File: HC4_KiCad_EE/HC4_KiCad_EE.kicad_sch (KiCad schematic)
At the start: 13 parts, among them IC2 ROM, J1 Power

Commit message: 仕様決め
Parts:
- added U1: ATmega4809-A, Package_QFP:TQFP-48_7x7mm_P0.5mm, symbol MCU_Microchip_ATmega:ATmega4809-A
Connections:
- new net: U1.14 (VCC), U1.42 (VCC)
- new net: U1.15 (GND), U1.29 (GND), U1.43 (GND)
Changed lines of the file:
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@@
+	)
+	(symbol
+		(lib_id "MCU_Microchip_ATmega:ATmega4809-A")
+		(at 52.07 96.52 0)
+		(unit 1)
+		(exclude_from_sim no)
+		(in_bom yes)
+		(on_board yes)
+		(dnp no)
+		(fields_autoplaced yes)
+		(property "Reference" "U1"
+			(at 54.2133 132.08 0)
+			(effects
+				(font
+					(size 1.27 1.27)
+				)
+				(justify left)
+			)
+		)
+		(property "Value" "ATmega4809-A"
+			(at 54.2133 134.62 0)
+			(effects
+				(font
+					(size 1.27 1.27)
+				)
+				(justify left)
+			)
+		)
+		(property "Footprint" "Package_QFP:TQFP-48_7x7mm_P0.5mm"
+			(at 52.07 96.52 0)
+			(effects
+				(font
+					(size 1.27 1.27)
+					(italic yes)
+				)
+				(hide yes)
+			)
+		)
+		(property "Datasheet" "http://ww1.microchip.com/downloads/en/DeviceDoc/40002016A.pdf"
+			(at 52.07 96.52 0)
+			(effects
+				(font
+					(size 1.27 1.27)
+				)
+				(hide yes)
+			)
+		)
+		(property "Description" "20MHz, 48kB Flash, 6kB SRAM, 256B EEPROM, TQFP-48"
+			(at 52.07 96.52 0)
+			(effects
+				(font
+					(size 1.27 1.27)
+				)
+				(hide yes)
+			)
+		)
+		(pin "32"
+		)
+		(pin "25"
+		)
+		(pin "21"
+		)
+		(pin "42"
+		)
+		(pin "29"
+		)
+		(pin "28"
+		)
+		(pin "34"
+		)
+		(pin "45"
+		)
+		(pin "37"
+		)
+		(pin "46"
+		)
+		(pin "31"
+		)
+		(pin "26"
+		)
+		(pin "40"
+		)
+		(pin "33"
+		)
+		(pin "35"
+		)
+		(pin "39"
+		)
+		(pin "41"
+		)
+		(pin "36"
+		)
+		(pin "30"
+		)
+		(pin "23"
+		)
+		(pin "38"
+		)
+		(pin "20"
+		)
+		(pin "22"
+		)
+		(pin "24"
+		)
+		(pin "27"
+		)
+		(pin "14"
+		)
+		(pin "15"
+		)
+		(pin "43"
+		)
+		(pin "44"
+		)
+		(pin "9"
+		)
+		(pin "11"
+		)
+		(pin "12"
+		)
+		(pin "47"
+		)
+		(pin "48"
+		)
+		(pin "8"
+		)
+		(pin "4"
+		)
+		(pin "13"
+		)
+		(pin "16"
+		)
+		(pin "10"
+		)
+		(pin "2"
+		)
+		(pin "3"
+		)
+		(pin "5"
+		)
+		(pin "6"
+		)
+		(pin "1"
+		)
+		(pin "7"
+		)
+		(pin "17"
+		)
+		(pin "18"
+		)
+		(pin "19"
+		)
+		(instances
+			(project ""
+				(path "/33731ded-38c0-4297-bdd8-92b082f46ff8"
+					(reference "U1")
+					(unit 1)
+				)
+			)
+		)
 	)
 	(symbol

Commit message: 一部を整地
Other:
- sheet Data BUS ports: added none; removed BUS_Zero, Databus[0..3], Level_C_OE, RAM_A[0..7], ~{RD}, ~{WR}
- sheet Instruction Decoder ports: added none; removed BUS_Zero, LevelC_OE
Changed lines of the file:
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@@
 	(bus
 		(pts
-			(xy 76.2 39.37) (xy 76.2 57.15)
-		)
-		(stroke
-			(width 0)
-			(type default)
-		)
-	)
-	(bus
-		(pts
 			(xy 254 71.12) (xy 254 93.98)
 		)
@@
 	(wire
 		(pts
-			(xy 60.96 49.53) (xy 60.96 39.37)
-		)
-		(stroke
-			(width 0)
-			(type default)
-		)
-	)
-	(bus
-		(pts
-			(xy 55.88 44.45) (xy 27.94 44.45)
-		)
-		(stroke
-			(width 0)
-			(type default)
-		)
-	)
-	(wire
-		(pts
 			(xy 43.18 171.45) (xy 48.26 171.45)
 		)
@@
 		)
 	)
-	(wire
-		(pts
-			(xy 203.2 39.37) (xy 203.2 48.26)
-		)
-		(stroke
-			(width 0)
-			(type default)
-		)
-	)
 	(polyline
 		(pts
@@
 		)
 	)
-	(bus
-		(pts
-			(xy 27.94 44.45) (xy 27.94 57.15)
-		)
-		(stroke
-			(width 0)
-			(type default)
-		)
-	)
 	(wire
 		(pts
@@
 		)
 	)
-	(wire
-		(pts
-			(xy 189.23 39.37) (xy 189.23 48.26)
-		)
-		(stroke
-			(width 0)
-			(type default)
-		)
-	)
 	(bus
 		(pts
@@
 	(bus
 		(pts
-			(xy 55.88 39.37) (xy 55.88 44.45)
-		)
-		(stroke
-			(width 0)
-			(type default)
-		)
-	)
-	(bus
-		(pts
 			(xy 116.84 81.28) (xy 116.84 83.82)
 		)
@@
 		)
 	)
-	(wire
-		(pts
-			(xy 58.42 39.37) (xy 58.42 52.07)
-		)
-		(stroke
-			(width 0)
-			(type default)
-		)
-	)
 	(bus
 		(pts
@@
 			)
 		)
-		(pin "BUS_Zero" input
-			(at 203.2 48.26 90)
-			(effects
-				(font
-					(size 1.27 1.27)
-				)
-				(justify right)
-			)
-		)
 		(pin "Zero_Flg" output
 			(at 238.76 59.69 0)
@@
 			)
 		)
-		(pin "LevelC_OE" output
-			(at 189.23 48.26 90)
-			(effects
-				(font
-					(size 1.27 1.27)
-				)
-				(justify right)
-			)
-		)
 		(pin "~{RAM_WR}" output
 			(at 201.93 76.2 270)
@@
 			)
 		)
-		(pin "ALU[0..3]" input
-			(at 91.44 39.37 270)
-			(effects
-				(font
-					(size 1.27 1.27)
-				)
-				(justify left)
-			)
-		)
-		(pin "Databus[0..3]" bidirectional
-			(at 76.2 39.37 270)
-			(effects
-				(font
-					(size 1.27 1.27)
-				)
-				(justify left)
-			)
-		)
 		(pin "Stack[0..3]" output
 			(at 105.41 39.37 270)
@@
 			)
 		)
-		(pin "~{ALU_OE}" input
-			(at 186.69 39.37 270)
-			(effects
-				(font
-					(size 1.27 1.27)
-				)
-				(justify left)
-			)
-		)
 		(pin "~{Immediate_OE}" input
 			(at 191.77 39.37 270)
@@
 			)
 		)
-		(pin "BUS_Zero" output
-			(at 203.2 39.37 270)
-			(effects
-				(font
-					(size 1.27 1.27)
-				)
-				(justify left)
-			)
-		)
-		(pin "RAM_A[0..7]" input
-			(at 55.88 39.37 270)
-			(effects
-				(font
-					(size 1.27 1.27)
-				)
-				(justify left)
-			)
-		)
-		(pin "~{RD}" input
-			(at 58.42 39.37 270)
-			(effects
-				(font
-					(size 1.27 1.27)
-				)
-				(justify left)
-			)
-		)
-		(pin "~{WR}" input
-			(at 60.96 39.37 270)
+		(pin "ALU[0..3]" input
+			(at 91.44 39.37 270)
 			(effects
 				(font
@@
 			)
 		)
-		(pin "Level_C_OE" input
-			(at 189.23 39.37 270)
+		(pin "~{ALU_OE}" input
+			(at 186.69 39.37 270)
 			(effects
 				(font

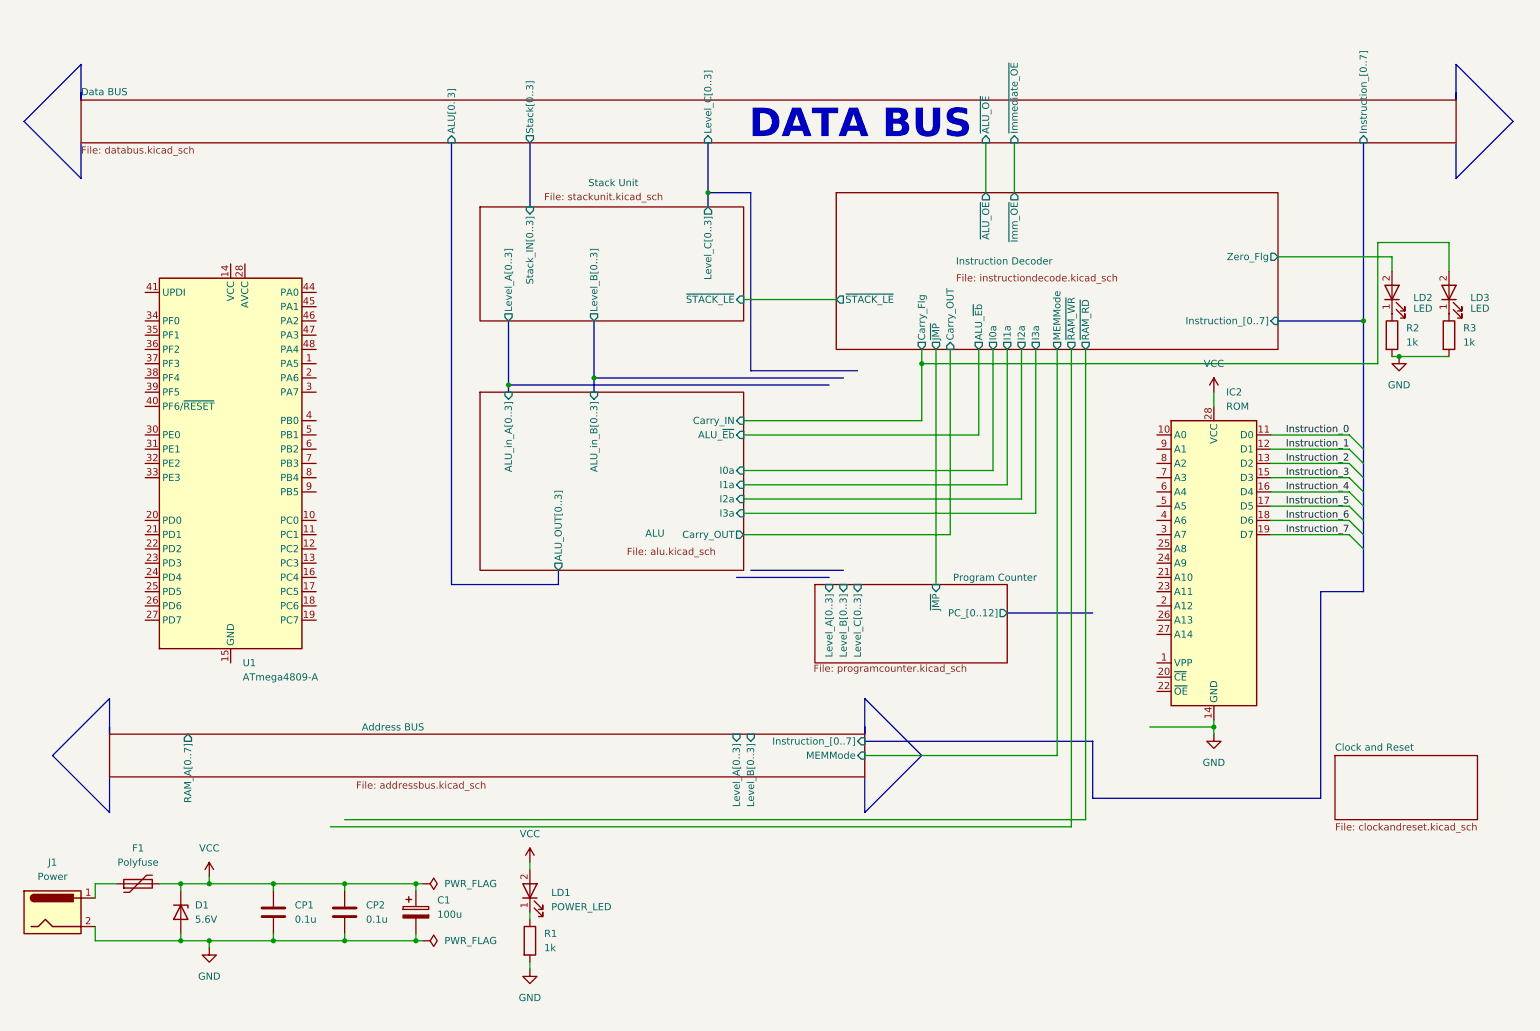
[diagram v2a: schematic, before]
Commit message: 4809を別シートに、ほか
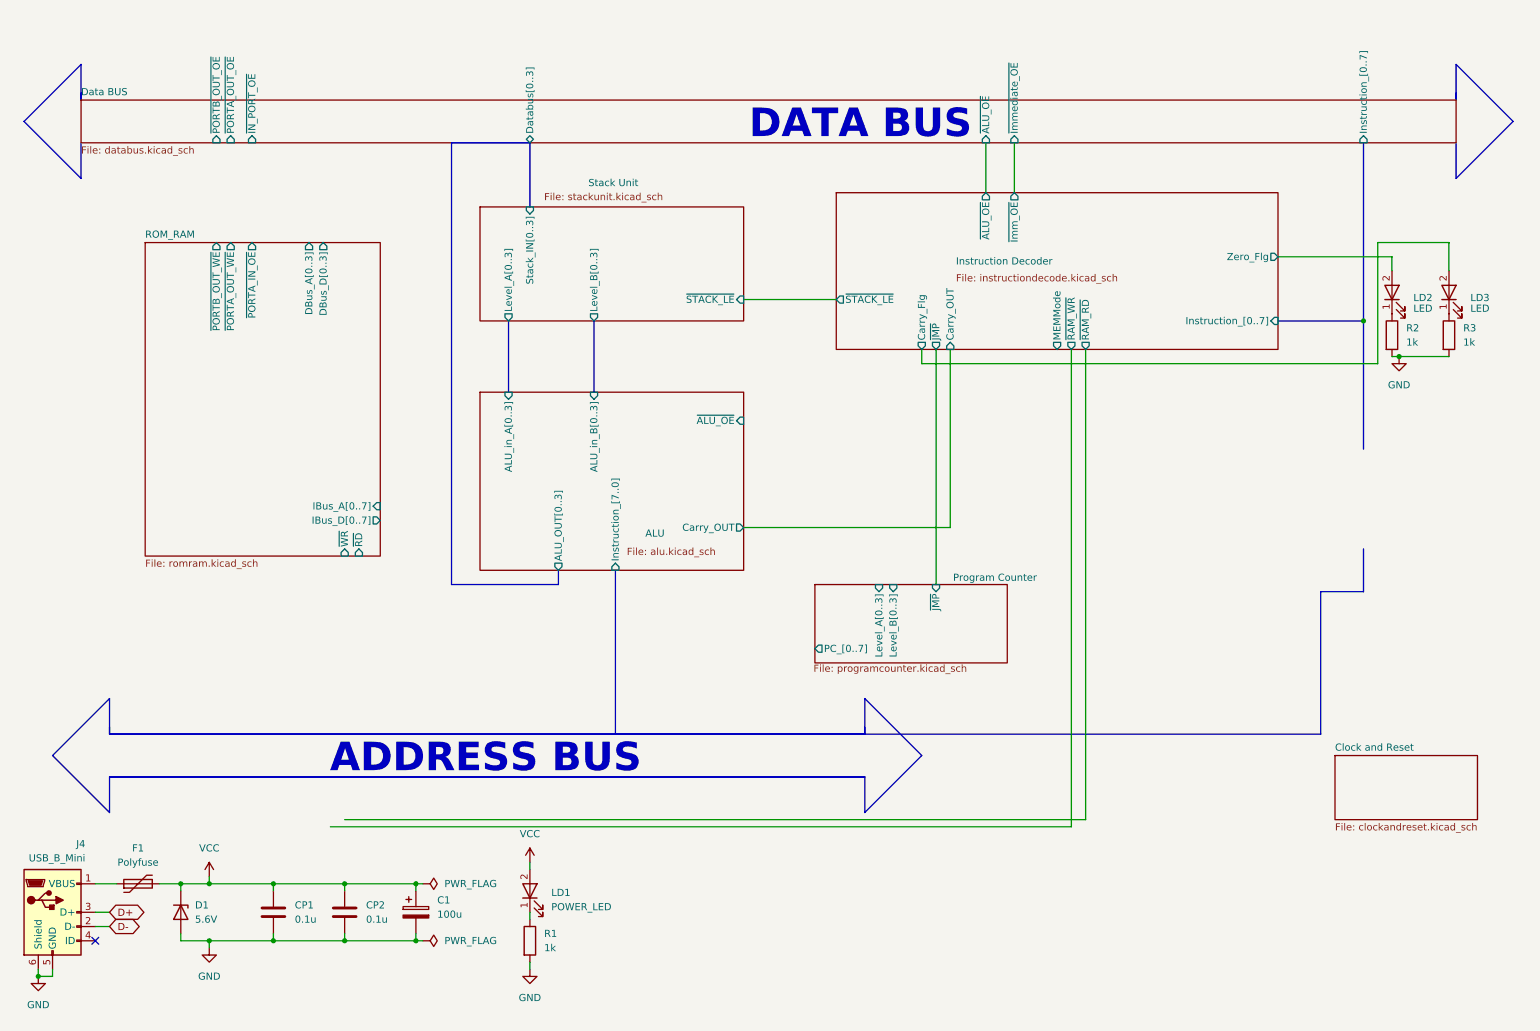
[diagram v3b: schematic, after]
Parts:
- removed IC2: ROM, Package_DIP:DIP-28_W15.24mm, symbol Memory_EPROM:27256
- removed J1: Power, Connector_BarrelJack:BarrelJack_GCT_DCJ200-10-A_Horizontal, symbol Connector:Barrel_Jack
- removed U1: ATmega4809-A, Package_QFP:TQFP-48_7x7mm_P0.5mm, symbol MCU_Microchip_ATmega:ATmega4809-A
- added J4: USB_B_Mini, symbol Connector:USB_B_Mini
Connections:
- net GND: now also J4.5 (GND), J4.6 (Shield)
- net at F1.1: now also J4.1 (VBUS)
- net ALU/Carry_IN renamed Instruction Decoder/Carry_Flg
- new net D+: J4.3 (D+)
- new net D-: J4.2 (D-)
- no-connect marks 0 -> 1
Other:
- removed sheet Address BUS
- added sheet ROM_RAM (romram.kicad_sch)
- sheet ALU ports: added Instruction_[7..0], ~{ALU_OE}; removed ALU_~{Eb}, Carry_IN, I0a, I1a, I2a, I3a
- sheet Data BUS ports: added Databus[0..3], ~{IN_PORT_OE}, ~{PORTA_OUT_OE}, ~{PORTB_OUT_OE}; removed ALU[0..3], Level_C[0..3], Stack[0..3]
- sheet Instruction Decoder ports: added none; removed ALU_~{Eb}, I0a, I1a, I2a, I3a
- sheet Program Counter ports: added PC_[0..7]; removed Level_C[0..3], PC_[0..12]
- sheet Stack Unit ports: added none; removed Level_C[0..3]
- note added: "ADDRESS BUS"

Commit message: 完成かも～
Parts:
- removed CP1, CP2: 0.1u, Capacitor_THT:C_Disc_D3.0mm_W1.6mm_P2.50mm, symbol Device2:C_Bypass
- removed D1: 5.6V, Diode_THT:D_DO-34_SOD68_P7.62mm_Horizontal, symbol Device:D_Zener
- removed LD2: LED, LED_THT:LED_Rectangular_W5.0mm_H2.0mm, symbol Device2:LED_
- removed R2: 1k, Resistor_THT:R_Axial_DIN0207_L6.3mm_D2.5mm_P7.62mm_Horizontal, symbol Device:R
- F1: value Polyfuse -> 500mA
- LD2: renamed from LD3; value LED -> Carry
- renumbered J4 to J1, R3 to R2
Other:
- sheet Data BUS ports: added none; removed ~{ALU_OE}, ~{Immediate_OE}
- sheet Instruction Decoder ports: added none; removed MEMMode, Zero_Flg, ~{Imm_OE}
- sheet ROM_RAM ports: added ~{PORT_IN_OE}; removed ~{PORTA_IN_OE}
- moved on the sheet: C1, LD2, R2

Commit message: ドキュメントを少々
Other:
- sheet Data BUS ports: added none; removed Instruction_[0..7]
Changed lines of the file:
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@@
-	)
-	(junction
-		(at 254 71.12)
-		(diameter 0)
-		(color 0 0 0 0)
 	)
 	(junction
@@
 		)
 	)
-	(bus
-		(pts
-			(xy 254 39.37) (xy 254 71.12)
-		)
-		(stroke
-			(width 0)
-			(type default)
-		)
-	)
-	(wire
-		(pts
-			(xy 201.93 161.29) (xy 69.85 161.29)
+	(wire
+		(pts
+			(xy 201.93 161.29) (xy 72.39 161.29)
 		)
 		(stroke
@@
 		)
 	)
+	(wire
+		(pts
+			(xy 74.93 113.03) (xy 74.93 160.02)
+		)
+		(stroke
+			(width 0)
+			(type default)
+		)
+	)
 	(polyline
 		(pts
@@
 	(wire
 		(pts
-			(xy 204.47 160.02) (xy 72.39 160.02)
+			(xy 204.47 160.02) (xy 74.93 160.02)
 		)
 		(stroke
@@
 		(pts
 			(xy 48.26 181.61) (xy 59.69 181.61)
+		)
+		(stroke
+			(width 0)
+			(type default)
+		)
+	)
+	(wire
+		(pts
+			(xy 72.39 113.03) (xy 72.39 161.29)
 		)
 		(stroke
@@
 			)
 		)
-		(pin "Instruction_[0..7]" input
-			(at 254 39.37 270)
-			(effects
-				(font
-					(size 1.27 1.27)
-				)
-				(justify left)
-			)
-		)

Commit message: PortBを4511に、フットプリントの割り付け開始
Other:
- sheet Data BUS ports: added Data_A[0..3]; removed none
- sheet Instruction Decoder ports: added Data_A[0..3]; removed none
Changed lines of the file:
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@@
+	)
+	(junction
+		(at 63.5 40.64)
+		(diameter 0)
+		(color 0 0 0 0)
 	)
 	(junction
@@
 	)
 	(junction
-		(at 59.69 181.61)
-		(diameter 0)
-		(color 0 0 0 0)
-	)
-	(junction
 		(at 59.69 171.45)
 		(diameter 0)
@@
 		)
 	)
+	(bus
+		(pts
+			(xy 63.5 40.64) (xy 161.29 40.64)
+		)
+		(stroke
+			(width 0)
+			(type default)
+		)
+	)
 	(polyline
 		(pts
@@
 	(wire
 		(pts
+			(xy 59.69 180.34) (xy 59.69 181.61)
+		)
+		(stroke
+			(width 0)
+			(type default)
+		)
+	)
+	(wire
+		(pts
 			(xy 20.32 187.96) (xy 17.78 187.96)
 		)
@@
 		)
 	)
+	(bus
+		(pts
+			(xy 63.5 40.64) (xy 63.5 57.15)
+		)
+		(stroke
+			(width 0)
+			(type default)
+		)
+	)
 	(polyline
 		(pts
@@
 	(bus
 		(pts
+			(xy 161.29 40.64) (xy 161.29 48.26)
+		)
+		(stroke
+			(width 0)
+			(type default)
+		)
+	)
+	(bus
+		(pts
 			(xy 170.18 118.11) (xy 170.18 80.01)
 		)
@@
 		)
 	)
-	(wire
-		(pts
-			(xy 60.96 181.61) (xy 59.69 181.61)
-		)
-		(stroke
-			(width 0)
-			(type default)
-		)
-	)
 	(bus
 		(pts
@@
 		)
 	)
+	(bus
+		(pts
+			(xy 63.5 39.37) (xy 63.5 40.64)
+		)
+		(stroke
+			(width 0)
+			(type default)
+		)
+	)
 	(wire
 		(pts
@@
 		(pts
 			(xy 25.4 30.48) (xy 25.4 31.75)
-		)
-		(stroke
-			(width 0)
-			(type default)
-		)
-	)
-	(wire
-		(pts
-			(xy 59.69 180.34) (xy 59.69 181.61)
 		)
 		(stroke
@@
 	)
 	(symbol
-		(lib_id "power:PWR_FLAG")
-		(at 60.96 181.61 270)
-		(unit 1)
-		(exclude_from_sim no)
-		(in_bom yes)
-		(on_board yes)
-		(dnp no)
-		(fields_autoplaced yes)
-		(property "Reference" "#FLG02"
-			(at 62.865 181.61 0)
-			(effects
-				(font
-					(size 1.27 1.27)
-				)
-				(hide yes)
-			)
-		)
-		(property "Value" "PWR_FLAG"
-			(at 64.77 181.6099 90)
-			(effects
-				(font
-					(size 1.27 1.27)
-				)
-				(justify left)
-			)
-		)
-		(property "Footprint" ""
-			(at 60.96 181.61 0)
-			(effects
-				(font
-					(size 1.27 1.27)
-				)
-				(hide yes)
-			)
-		)
-		(property "Datasheet" "~"
-			(at 60.96 181.61 0)
-			(effects
-				(font
-					(size 1.27 1.27)
-				)
-				(hide yes)
-			)
-		)
-		(property "Description" "Special symbol for telling ERC where power comes from"
-			(at 60.96 181.61 0)
-			(effects
-				(font
-					(size 1.27 1.27)
-				)
-				(hide yes)
-			)
-		)
-		(pin "1"
-		)
-		(instances
-			(project "HC4_KiCad"
-				(path "/33731ded-38c0-4297-bdd8-92b082f46ff8"
-					(reference "#FLG02")
-					(unit 1)
-				)
-			)
-		)
-	)
-	(symbol
 		(lib_id "power:VCC")
 		(at 105.41 167.64 0)
@@
 			)
 		)
+		(pin "Data_A[0..3]" output
+			(at 161.29 48.26 90)
+			(effects
+				(font
+					(size 1.27 1.27)
+				)
+				(justify right)
+			)
+		)
 		(instances
 			(project "HC4_KiCad_EE"
@@
 			(effects
 				(font
+					(size 1.27 1.27)
+				)
+				(justify left)
+			)
+		)
+		(pin "Data_A[0..3]" input
+			(at 63.5 39.37 270)
+			(effects
+				(font

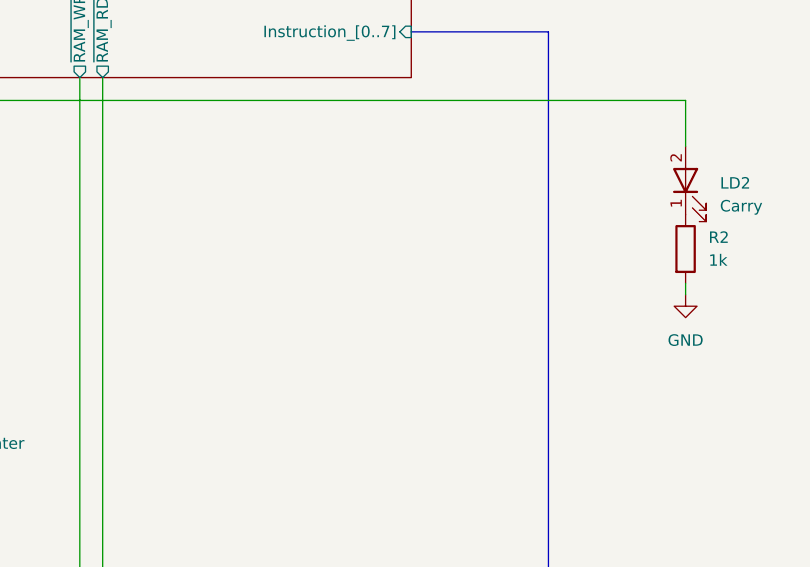
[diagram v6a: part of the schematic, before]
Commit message: チップ集合抵抗に変更、基板作成開始
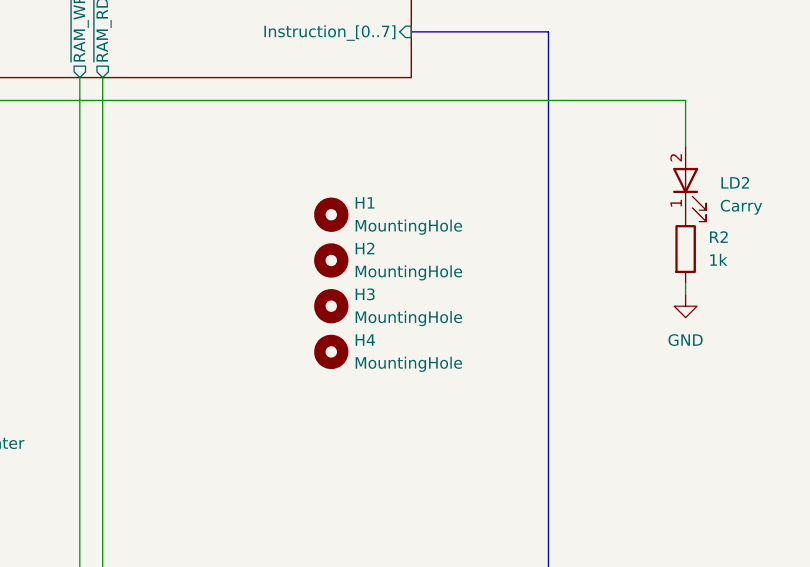
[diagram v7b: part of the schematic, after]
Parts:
- added H1, H2, H3, H4: MountingHole, MountingHole:MountingHole_3.2mm_M3, symbol Mechanical:MountingHole
- J1: footprint (none) -> Connector_USB:USB_Mini-B_Wuerth_65100516121_Horizontal
- R1, R2: footprint Resistor_THT:R_Axial_DIN0207_L6.3mm_D2.5mm_P7.62mm_Horizontal -> Resistor_SMD:R_0603_1608Metric

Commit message: 自動配線前最終チェック
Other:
- sheet Data BUS ports: added ~{PORTA_OUT_WE}, ~{PORTB_OUT_WE}; removed ~{PORTA_OUT_OE}, ~{PORTB_OUT_OE}
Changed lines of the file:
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@@
 	(wire
 		(pts
-			(xy 201.93 161.29) (xy 72.39 161.29)
+			(xy 72.39 161.29) (xy 201.93 161.29)
 		)
 		(stroke
@@
 	(wire
 		(pts
-			(xy 204.47 160.02) (xy 74.93 160.02)
+			(xy 74.93 160.02) (xy 204.47 160.02)
 		)
 		(stroke
@@
 			)
 		)
-		(pin "~{PORTB_OUT_OE}" input
-			(at 49.53 39.37 270)
-			(effects
-				(font
-					(size 1.27 1.27)
-				)
-				(justify left)
-			)
-		)
-		(pin "~{PORTA_OUT_OE}" input
-			(at 52.07 39.37 270)
-			(effects
-				(font
-					(size 1.27 1.27)
-				)
-				(justify left)
-			)
-		)
 		(pin "~{IN_PORT_OE}" input
 			(at 55.88 39.37 270)
@@
 			(effects
 				(font
+					(size 1.27 1.27)
+				)
+				(justify left)
+			)
+		)
+		(pin "~{PORTA_OUT_WE}" input
+			(at 52.07 39.37 270)
+			(effects
+				(font
+					(size 1.27 1.27)
+				)
+				(justify left)
+			)
+		)
+		(pin "~{PORTB_OUT_WE}" input
+			(at 49.53 39.37 270)
+			(effects
+				(font
